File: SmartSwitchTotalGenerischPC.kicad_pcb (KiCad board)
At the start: 2 copper layers, 21.5 x 32 mm, 12 parts, among them J1 Conn_02x05_Odd_Even, J2 Conn_02x05_Odd_Even, J3 Conn_02x04_Odd_Even, Q1 SS8050, U1 XIAO-ESP32-C6

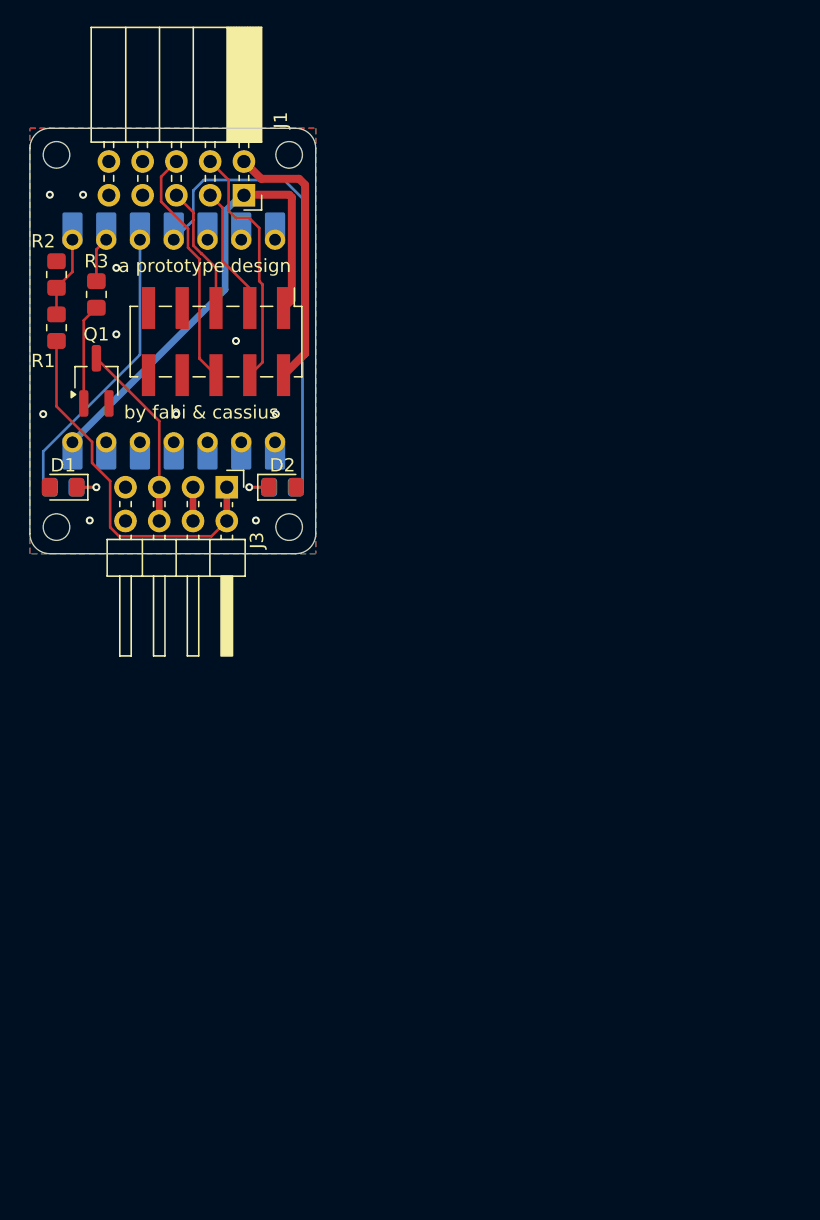
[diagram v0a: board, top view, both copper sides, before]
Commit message: refactor: redesign system, replaced BJT w. optocoupler, new input RST_SW
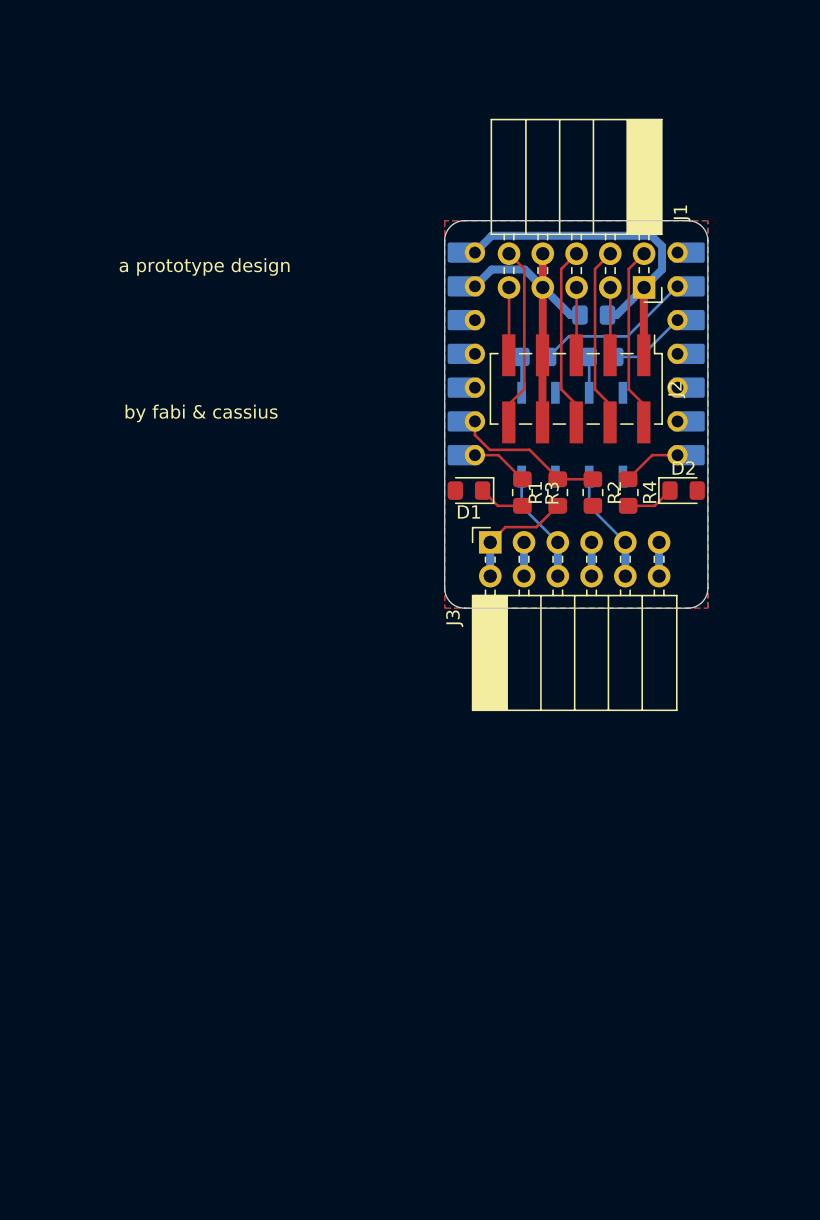
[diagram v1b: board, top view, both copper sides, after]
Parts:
- removed Q1: SS8050, Package_TO_SOT_SMD:SOT-23W_Handsoldering
- added C1: 100n, Capacitor_SMD:C_0805_2012Metric_Pad1.18x1.45mm_HandSolder, B.Cu at (153.4, 51.0)
- added IC1: AQW282SZ, Footprints:SOP254P680X230-8N, B.Cu at (151.8, 60.0)
- added R6: 1k, Resistor_SMD:R_0805_2012Metric_Pad1.20x1.40mm_HandSolder, B.Cu at (149.0, 54.2)
- J3: value Conn_02x04_Odd_Even -> Conn_02x06_Odd_Even; footprint Connector_PinHeader_2.54mm:PinHeader_2x04_P2.54mm_Horizontal -> Connector_PinSocket_2.54mm:PinSocket_2x06_P2.54mm_Horizontal
- R3: value 3.3k -> R
- R4: moved to F.Cu
- R5: value R -> 1k
- moved R2 43.6 mm to (153.3, 64.4), turned to -90 degrees
- moved R4 42.5 mm to (156.0, 64.4), turned to -90 degrees
- moved R1 39.7 mm to (150.7, 64.4)
- moved R3 35.3 mm to (148.1, 64.4), turned to -90 degrees
- moved J1 30.9 mm to (157.2, 49.0)
- moved D1 30.5 mm to (144.0, 64.2)
- moved U1 30.2 mm to (152.1, 54.0), turned to 180 degrees
- moved D2 30.2 mm to (160.2, 64.2)
- moved J2 27.3 mm to (152.1, 56.6)
- moved R5 26.0 mm to (154.1, 54.2)
- moved J3 20.2 mm to (145.6, 68.2), turned to 90 degrees
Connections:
- R1 pad 2: Net-(U1-GPIO0/A0/D0) -> /GPIO19
- R2 pad 1: Net-(U1-GPIO0/A0/D0) -> /GPIO19
- R3 pad 1: Net-(Q1-B) -> /GPIO17
- R3 pad 2: Net-(U1-GPIO1/A1/D1) -> Net-(D1-K)
- R4 pad 1: Net-(U1-GPIO2/A2/D2) -> /GPIO16
- R4 pad 2: Net-(D1-K) -> Net-(D2-K)
- R5 pad 1: Net-(U1-GPIO21/D3) -> /GPIO2
- R5 pad 2: Net-(D2-K) -> Net-(IC1-A2)
- U1 pad 1: Net-(U1-GPIO0/A0/D0) -> unconnected-(U1-GPIO0/A0/D0-Pad1)
- U1 pad 2: Net-(U1-GPIO1/A1/D1) -> /GPIO1
- U1 pad 3: Net-(U1-GPIO2/A2/D2) -> /GPIO2
- U1 pad 4: Net-(U1-GPIO21/D3) -> unconnected-(U1-GPIO21/D3-Pad4)
- U1 pad 7: unconnected-(U1-GPIO16/D6/TX-Pad7)_1 -> /GPIO16
- U1 pad 8: unconnected-(U1-GPIO17/D7/RX-Pad8)_1 -> /GPIO17
- U1 pad 9: unconnected-(U1-GPIO19/D8/SCK-Pad9)_1 -> /GPIO19
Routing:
- net Net-(U1-GPIO21/D3): track 35.4 -> 0.00 mm
- net GND: track 2.59 -> 28.8 mm, vias 10 -> 0
- net Net-(U1-GPIO2/A2/D2): track 21.8 -> 0.00 mm
- net /PWR_LED+: track 27.8 -> 8.75 mm
- net /GPIO1: track 0.00 -> 15.7 mm
- net unconnected-(J1-NC-Pad10): track 0.00 -> 12.3 mm
- net /GPIO19: track 0.00 -> 11.3 mm
- net +5V: track 36.3 -> 26.0 mm
- net /RST_SW+: track 0.00 -> 8.62 mm
- net Net-(J1-USB1_5V): track 20.4 -> 12.3 mm
- net Net-(Q1-B): track 7.59 -> 0.00 mm
- net Net-(J1-USB1_D-): track 18.7 -> 12.3 mm
- net Net-(U1-GPIO0/A0/D0): track 6.12 -> 0.00 mm
- net Net-(J1-USB1_D+): track 18.3 -> 12.3 mm
- net Net-(J1-USB0_D+): track 9.72 -> 3.76 mm
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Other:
- board size 21.5 x 32 mm -> 19.8 x 29.1 mm

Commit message: revised: GND plane
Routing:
- net GND: track 28.8 -> 0.00 mm
- net /PWR_LED+: track 8.75 -> 2.54 mm
- net (no net): track 0.00 -> 5.11 mm
- net /GPIO1: track 15.7 -> 11.9 mm
- net Net-(IC1-A2): track 2.71 -> 0.00 mm
- net Net-(IC1-A1): track 2.70 -> 0.00 mm
- net Net-(J1-USB0_D+): track 3.76 -> 5.11 mm
- net unconnected-(J1-NC-Pad10): track 12.3 -> 13.7 mm
- net Net-(J1-USB0_D-): track 3.76 -> 5.11 mm
- net Net-(J1-USB1_5V): track 12.3 -> 13.6 mm
- net Net-(J1-USB1_D-): track 12.3 -> 13.6 mm
- net Net-(J1-USB1_D+): track 12.3 -> 13.6 mm
- net /GPIO2: vias 0 -> 1

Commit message: addition: stitching vias
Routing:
- net unconnected-(J2-NC-Pad10): track 0.00 -> 13.7 mm
- net unconnected-(J1-NC-Pad10): track 13.7 -> 0.00 mm
- net GND: vias 0 -> 25
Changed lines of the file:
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@@
 		(net "/PWR_LED+")
+	)
+	(via
+		(at 148.3 61.1)
+		(size 0.6)
+		(drill 0.3)
+		(layers "F.Cu" "B.Cu")
+		(free yes)
+		(net "GND")
+	)
+	(via
+		(at 144 63)
+		(size 0.6)
+		(drill 0.3)
+		(layers "F.Cu" "B.Cu")
+		(free yes)
+		(net "GND")
+	)
+	(via
+		(at 145.9 50.4)
+		(size 0.6)
+		(drill 0.3)
+		(layers "F.Cu" "B.Cu")
+		(free yes)
+		(net "GND")
+	)
+	(via
+		(at 150.65 61.4)
+		(size 0.6)
+		(drill 0.3)
+		(layers "F.Cu" "B.Cu")
+		(free yes)
+		(net "GND")
+	)
+	(via
+		(at 143.25 66.1)
+		(size 0.6)
+		(drill 0.3)
+		(layers "F.Cu" "B.Cu")
+		(free yes)
+		(net "GND")
+	)
+	(via
+		(at 151.9 61.8)
+		(size 0.6)
+		(drill 0.3)
+		(layers "F.Cu" "B.Cu")
+		(free yes)
+		(net "GND")
+	)
+	(via
+		(at 160.7 69.3)
+		(size 0.6)
+		(drill 0.3)
+		(layers "F.Cu" "B.Cu")
+		(free yes)
+		(net "GND")
+	)
+	(via
+		(at 149.6 51.1)
+		(size 0.6)
+		(drill 0.3)
+		(layers "F.Cu" "B.Cu")
+		(free yes)
+		(net "GND")
+	)
+	(via
+		(at 143.55 71.05)
+		(size 0.6)
+		(drill 0.3)
+		(layers "F.Cu" "B.Cu")
+		(free yes)
+		(net "GND")
+	)
+	(via
+		(at 146.5 56.55)
+		(size 0.6)
+		(drill 0.3)
+		(layers "F.Cu" "B.Cu")
+		(free yes)
+		(net "GND")
+	)
+	(via
+		(at 161.3 67.8)
+		(size 0.6)
+		(drill 0.3)
+		(layers "F.Cu" "B.Cu")
+		(free yes)
+		(net "GND")
+	)
+	(via
+		(at 157.7 56.6)
+		(size 0.6)
+		(drill 0.3)
+		(layers "F.Cu" "B.Cu")
+		(free yes)
+		(net "GND")
+	)
+	(via
+		(at 157.8 65.45)
+		(size 0.6)
+		(drill 0.3)
+		(layers "F.Cu" "B.Cu")
+		(free yes)
+		(net "GND")
+	)
+	(via
+		(at 160.65 66.65)
+		(size 0.6)
+		(drill 0.3)
+		(layers "F.Cu" "B.Cu")
+		(free yes)
+		(net "GND")
+	)
+	(via
+		(at 159.35 65.85)
+		(size 0.6)
+		(drill 0.3)
+		(layers "F.Cu" "B.Cu")
+		(free yes)
+		(net "GND")
+	)
+	(via
+		(at 155.95 61.2)
+		(size 0.6)
+		(drill 0.3)
+		(layers "F.Cu" "B.Cu")
+		(free yes)
+		(net "GND")
+	)
+	(via
+		(at 157.45 61.75)
+		(size 0.6)
+		(drill 0.3)
+		(layers "F.Cu" "B.Cu")
+		(free yes)
+		(net "GND")
+	)
+	(via
+		(at 143.15 69.15)
+		(size 0.6)
+		(drill 0.3)
+		(layers "F.Cu" "B.Cu")
+		(free yes)
+		(net "GND")
+	)
+	(via
+		(at 145.1 65.95)
+		(size 0.6)
+		(drill 0.3)
+		(layers "F.Cu" "B.Cu")
+		(free yes)
+		(net "GND")
+	)
+	(via
+		(at 161 71.05)
+		(size 0.6)
+		(drill 0.3)
+		(layers "F.Cu" "B.Cu")
+		(free yes)
+		(net "GND")
+	)
+	(via
+		(at 143.65 67.3)
+		(size 0.6)
+		(drill 0.3)
+		(layers "F.Cu" "B.Cu")
+		(free yes)
+		(net "GND")
+	)
+	(via
+		(at 160.25 63.05)
+		(size 0.6)
+		(drill 0.3)
+		(layers "F.Cu" "B.Cu")
+		(free yes)
+		(net "GND")
+	)
+	(via
+		(at 158.6 55.2)
+		(size 0.6)
+		(drill 0.3)
+		(layers "F.Cu" "B.Cu")
+		(free yes)
+		(net "GND")
+	)
+	(via
+		(at 153.35 61.35)
+		(size 0.6)
+		(drill 0.3)
+		(layers "F.Cu" "B.Cu")
+		(free yes)
+		(net "GND")
+	)
+	(via
+		(at 154.3 61.85)
+		(size 0.6)
+		(drill 0.3)
+		(layers "F.Cu" "B.Cu")
+		(free yes)
+		(net "GND")
 	)
 	(segment
@@
 		(width 0.2)
 		(layer "F.Cu")
-		(net "unconnected-(J1-NC-Pad10)")
+		(net "unconnected-(J2-NC-Pad10)")
 	)
 	(segment
@@
 		(width 0.2)
 		(layer "F.Cu")
-		(net "unconnected-(J1-NC-Pad10)")
+		(net "unconnected-(J2-NC-Pad10)")
 	)
 	(segment
@@
 		(width 0.2)
 		(layer "F.Cu")
-		(net "unconnected-(J1-NC-Pad10)")
-	)
-	(segment
+		(net "unconnected-(J2-NC-Pad10)")
+	)
+	(segment

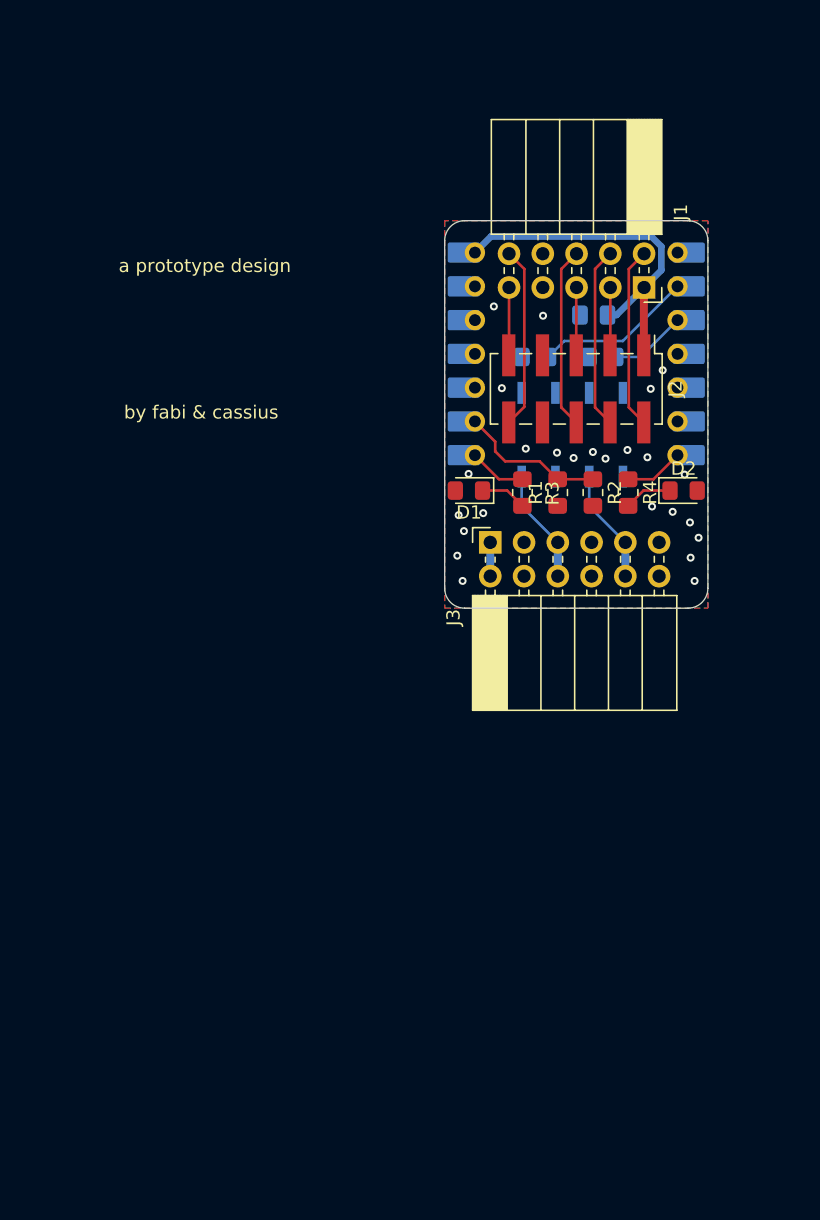
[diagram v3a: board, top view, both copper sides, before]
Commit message: WIP: revised layout w. specific component positions, replaced 2x6 header with 2x6 pin
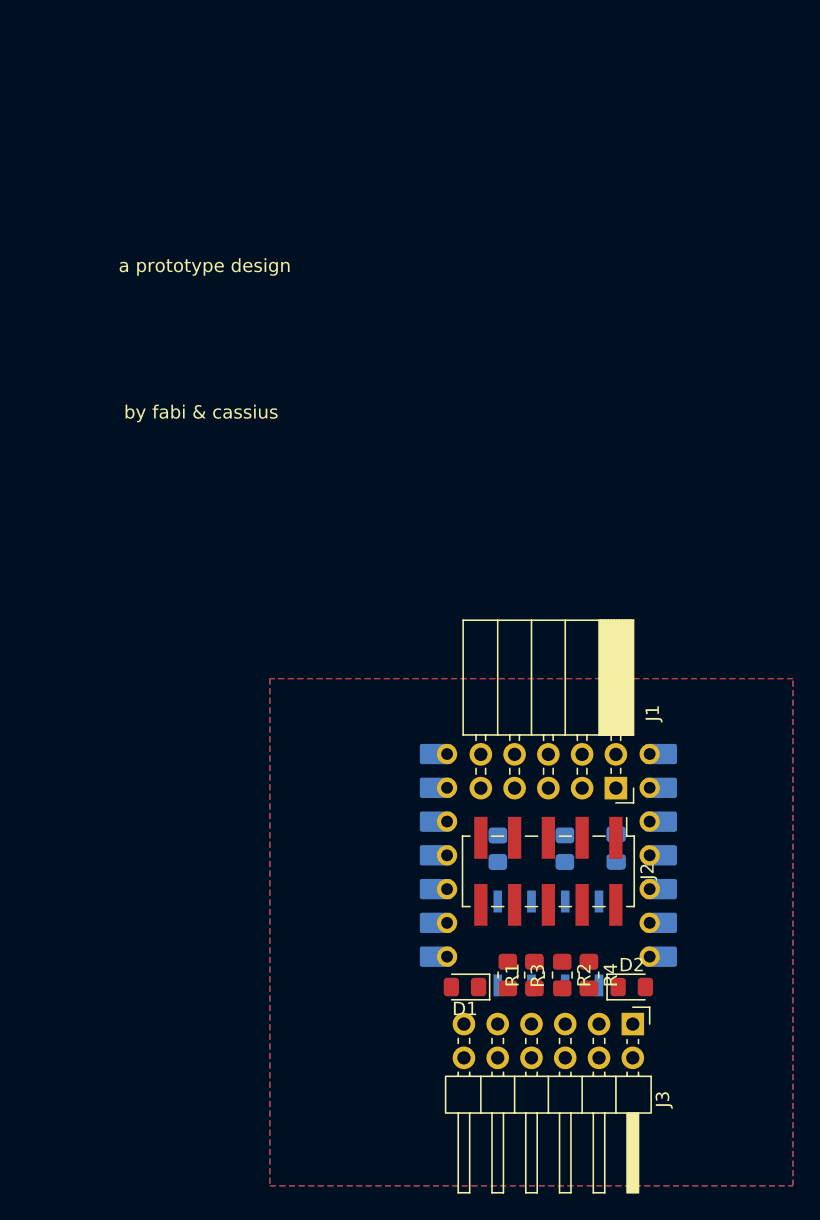
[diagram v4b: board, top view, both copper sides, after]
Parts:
- J3: footprint Connector_PinSocket_2.54mm:PinSocket_2x06_P2.54mm_Horizontal -> Connector_PinHeader_2.54mm:PinHeader_2x06_P2.54mm_Horizontal
- moved C1 40.1 mm to (155.1, 91.1), turned to -90 degrees
- moved IC1 38.3 mm to (150.0, 98.3)
- moved J3 37.8 mm to (156.3, 104.4), turned to -90 degrees
- moved U1 37.8 mm to (150.0, 91.7)
- moved J1 37.7 mm to (155.1, 86.6)
- moved D2 37.5 mm to (156.3, 101.6)
- moved D1 37.3 mm to (143.7, 101.6)
- moved R6 37.1 mm to (146.2, 91.2), turned to -90 degrees
- moved R5 37.1 mm to (151.2, 91.2), turned to -90 degrees
- moved R4 36.4 mm to (153.1, 100.7)
- moved R2 36.4 mm to (151.1, 100.7)
- moved J2 36.4 mm to (150.0, 92.9)
- moved R1 36.3 mm to (148.9, 100.7)
- moved R3 36.3 mm to (146.9, 100.7)
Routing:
- net +5V: track 25.8 -> 0.00 mm
- net unconnected-(J2-NC-Pad10): track 13.7 -> 0.00 mm
- net Net-(J1-USB1_D-): track 13.6 -> 0.00 mm
- net Net-(J1-USB1_D+): track 13.6 -> 0.00 mm
- net Net-(J1-USB1_5V): track 13.6 -> 0.00 mm
- net /GPIO1: track 11.9 -> 0.00 mm
- net /GPIO19: track 11.1 -> 0.00 mm
- net /RST_SW+: track 8.62 -> 0.00 mm
- net /PWR_SW+: track 8.62 -> 0.00 mm
- net /GPIO2: track 5.81 -> 0.00 mm, vias 1 -> 0
- net Net-(J1-USB0_D+): track 5.11 -> 0.00 mm
- net Net-(J1-USB0_D-): track 5.11 -> 0.00 mm
- net (no net): track 5.11 -> 0.00 mm
- net /GPIO16: track 4.46 -> 0.00 mm
- net /GPIO17: track 4.32 -> 0.00 mm
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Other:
- board outline removed

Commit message: revised: edge cut, silkscreen, machining points, component placement. addition: pulldown resistors f. optocoupler
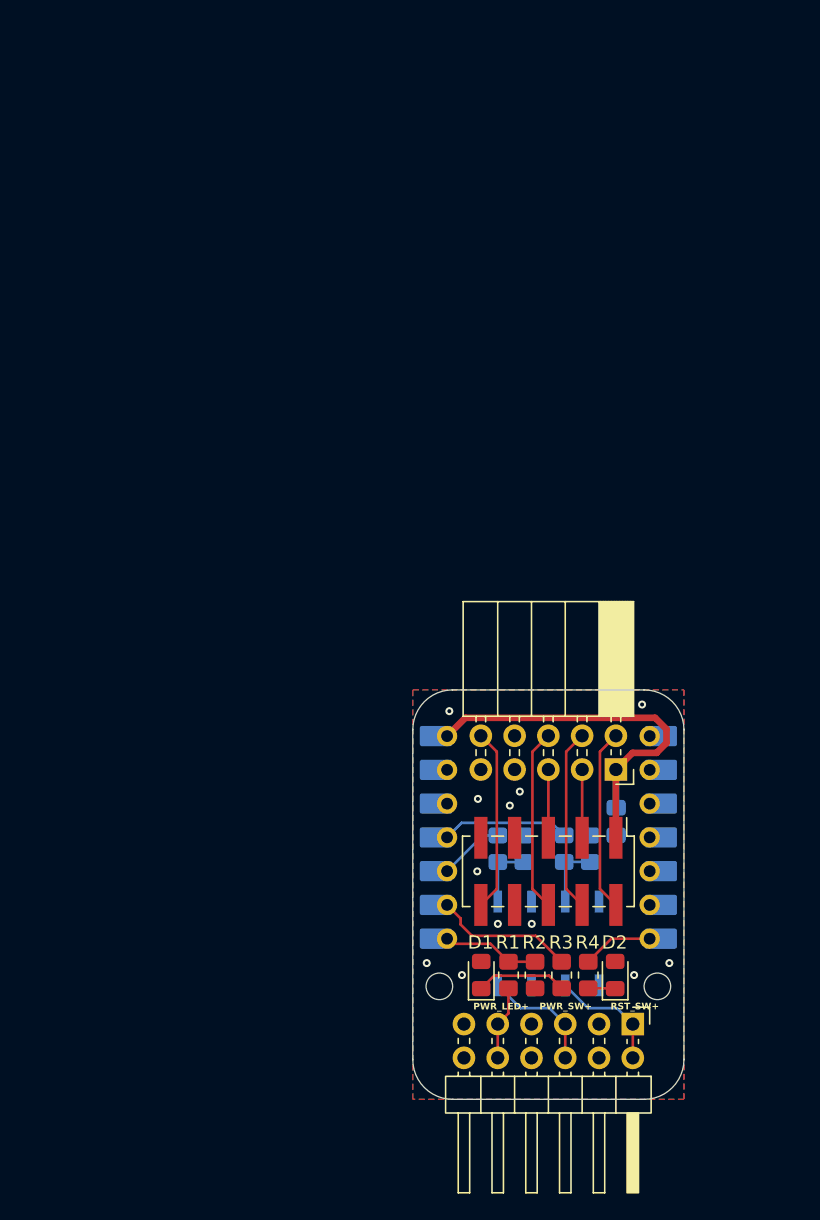
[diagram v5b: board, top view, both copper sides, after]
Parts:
- added R7: 10k, Resistor_SMD:R_0805_2012Metric_Pad1.20x1.40mm_HandSolder, B.Cu at (153.2, 91.2)
- added R8: 10k, Resistor_SMD:R_0805_2012Metric_Pad1.20x1.40mm_HandSolder, B.Cu at (148.2, 91.2)
- moved R3 4.05 mm to (151.0, 100.7)
- moved R2 2.05 mm to (149.0, 100.7)
- moved C1 2.00 mm to (155.1, 89.1)
- moved R1 1.95 mm to (147.0, 100.7)
- moved D2 1.54 mm to (155.0, 100.7), turned to 90 degrees
- moved D1 1.52 mm to (144.9, 100.7), turned to 90 degrees
- moved J1 1.40 mm to (155.1, 85.2)
- moved U1 1.35 mm to (150.0, 90.3)
- moved R4 0.05 mm to (153.0, 100.7)
- moved R5 0.05 mm to (151.2, 91.2)
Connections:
- J3 pad 1: /PWR_LED+ -> /RST_SW+
- J3 pad 10: /RST_SW+ -> /PWR_LED+
- J3 pad 2: /PWR_LED+ -> /RST_SW+
- J3 pad 9: /RST_SW+ -> /PWR_LED+
- R1 pad 2: /GPIO19 -> /GPIO17
- R2 pad 1: /GPIO19 -> /GPIO17
- R3 pad 1: /GPIO17 -> /GPIO19
- R5 pad 1: /GPIO2 -> /GPIO18
- R6 pad 1: /GPIO1 -> /GPIO20
- U1 pad 10: unconnected-(U1-GPIO20/D9/MISO-Pad10) -> /GPIO20
- U1 pad 11: unconnected-(U1-GPIO18/D10/MOSI-Pad11) -> /GPIO18
- U1 pad 2: /GPIO1 -> unconnected-(U1-GPIO1/A1/D1-Pad2)_1
- U1 pad 3: /GPIO2 -> unconnected-(U1-GPIO2/A2/D2-Pad3)
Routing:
- net +5V: track 0.00 -> 31.1 mm
- net unconnected-(J1-NC-Pad10): track 0.00 -> 13.7 mm
- net Net-(J1-USB1_5V): track 0.00 -> 13.7 mm
- net Net-(J1-USB1_D-): track 0.00 -> 13.7 mm
- net Net-(J1-USB1_D+): track 0.00 -> 13.7 mm
- net /GPIO19: track 0.00 -> 10.7 mm
- net /GPIO18: track 0.00 -> 9.66 mm
- net /PWR_SW+: track 0.00 -> 8.83 mm
- net /RST_SW+: track 0.00 -> 8.83 mm
- net /GPIO17: track 0.00 -> 7.34 mm
- net Net-(D1-K): track 0.00 -> 6.85 mm
- net /PWR_LED+: track 0.00 -> 5.56 mm
- net /GPIO16: track 0.00 -> 5.34 mm
- net Net-(J1-USB0_D-): track 0.00 -> 5.13 mm
- net Net-(J1-USB0_D+): track 0.00 -> 5.13 mm
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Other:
- board outline added: 20.4 x 30.8 mm
- board text added: "PWR_LED+"
- board text added: "PWR_SW+"
- board text added: "RST_SW+"
- board text removed: "a prototype design"
- board text removed: "by fabi & cassius"
